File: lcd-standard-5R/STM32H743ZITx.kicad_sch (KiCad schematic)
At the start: 37 parts, among them J2 SWD, J3 Conn_ARM_JTAG_SWD_10, SW1 SW_Push, SW2 SW_Push, U10 STM32H743ZITx, Y1 25MHz, Y2 32.768KHz

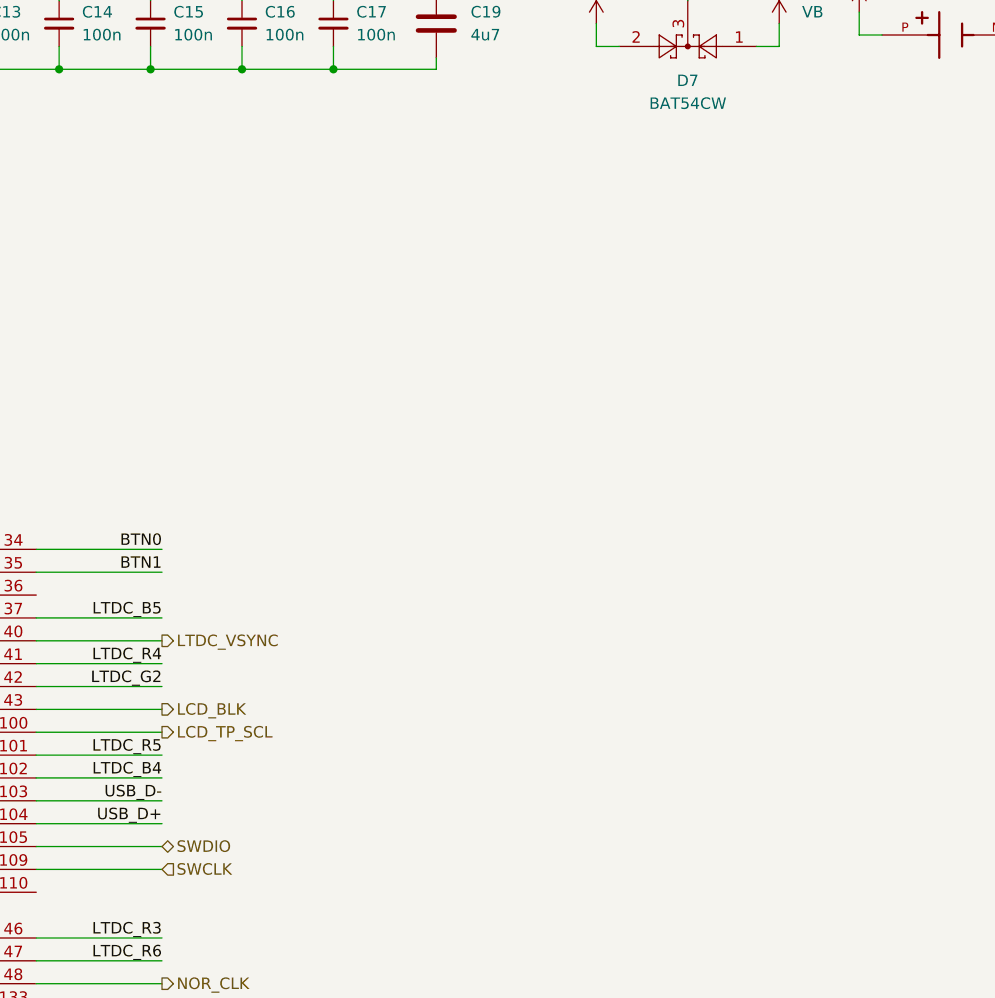
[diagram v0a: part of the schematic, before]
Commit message: Change MCU to STM32H743
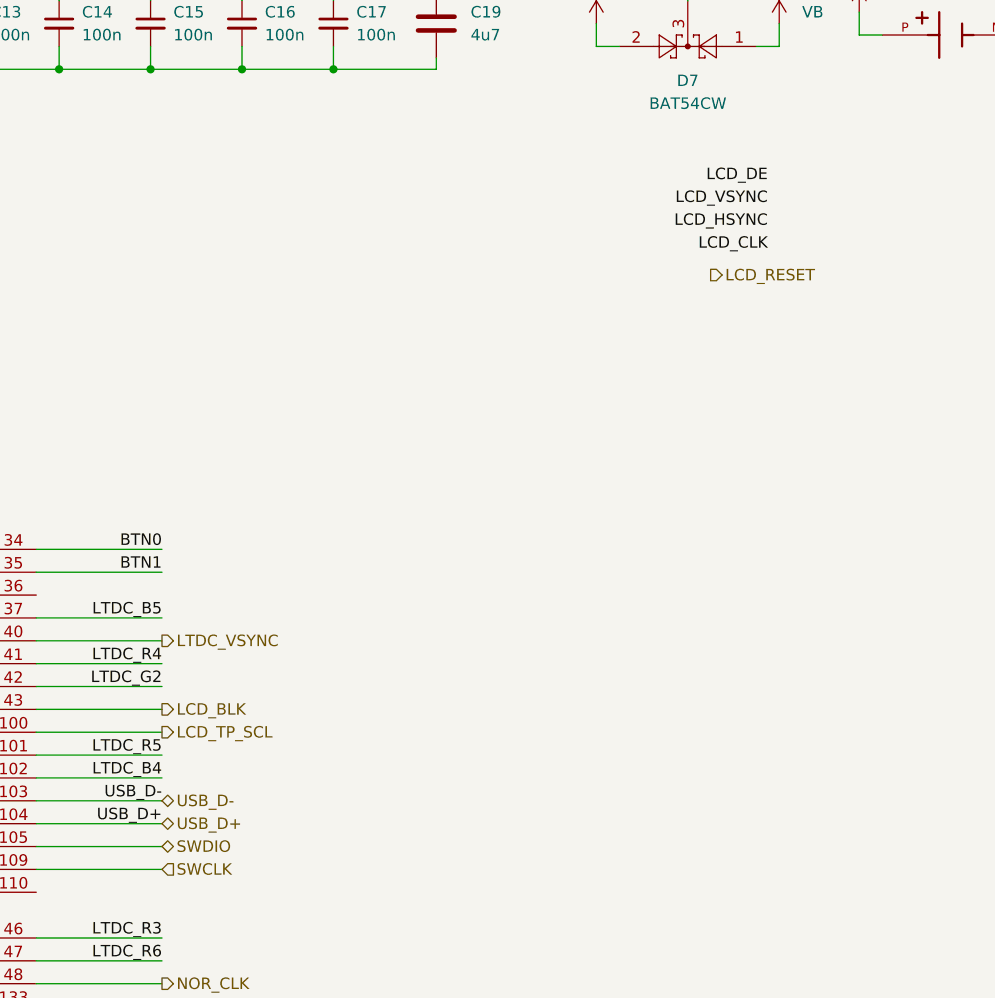
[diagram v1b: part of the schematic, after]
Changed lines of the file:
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@@
+		)
+	)
+	(label "LCD_VSYNC"
+		(at 195.58 53.34 180)
+		(fields_autoplaced yes)
+		(effects
+			(font
+				(size 1.27 1.27)
+			)
+			(justify right bottom)
 		)
 	)
@@
 		)
 	)
+	(label "LCD_DE"
+		(at 195.58 50.8 180)
+		(fields_autoplaced yes)
+		(effects
+			(font
+				(size 1.27 1.27)
+			)
+			(justify right bottom)
+		)
+	)
 	(label "LTDC_B4"
 		(at 128.27 116.84 180)
@@
 		)
 	)
+	(label "LCD_HSYNC"
+		(at 195.58 55.88 180)
+		(fields_autoplaced yes)
+		(effects
+			(font
+				(size 1.27 1.27)
+			)
+			(justify right bottom)
+		)
+	)
 	(label "OSC32_IN"
 		(at 144.78 228.6 0)
@@
 	(label "~{SDRAM_RAS}"
 		(at 283.21 60.96 180)
+		(fields_autoplaced yes)
+		(effects
+			(font
+				(size 1.27 1.27)
+			)
+			(justify right bottom)
+		)
+	)
+	(label "LCD_CLK"
+		(at 195.58 58.42 180)
 		(fields_autoplaced yes)
 		(effects
@@
 		)
 	)
+	(hierarchical_label "LCD_RESET"
+		(shape output)
+		(at 189.23 60.96 0)
+		(fields_autoplaced yes)
+		(effects
+			(font
+				(size 1.27 1.27)
+			)
+			(justify left)
+		)
+	)
 	(hierarchical_label "LTDC_G[2..7]"
 		(shape output)
@@
 		(fields_autoplaced yes)
 		(effects
+			(font
+				(size 1.27 1.27)
+			)
+			(justify left)
+		)
+	)
+	(hierarchical_label "USB_D+"
+		(shape bidirectional)
+		(at 128.27 121.92 0)
+		(fields_autoplaced yes)
+		(effects
+			(font
+				(size 1.27 1.27)
+			)
+			(justify left)
+		)
+	)
+	(hierarchical_label "USB_D-"
+		(shape bidirectional)
+		(at 128.27 119.38 0)
+		(fields_autoplaced yes)
+		(effects

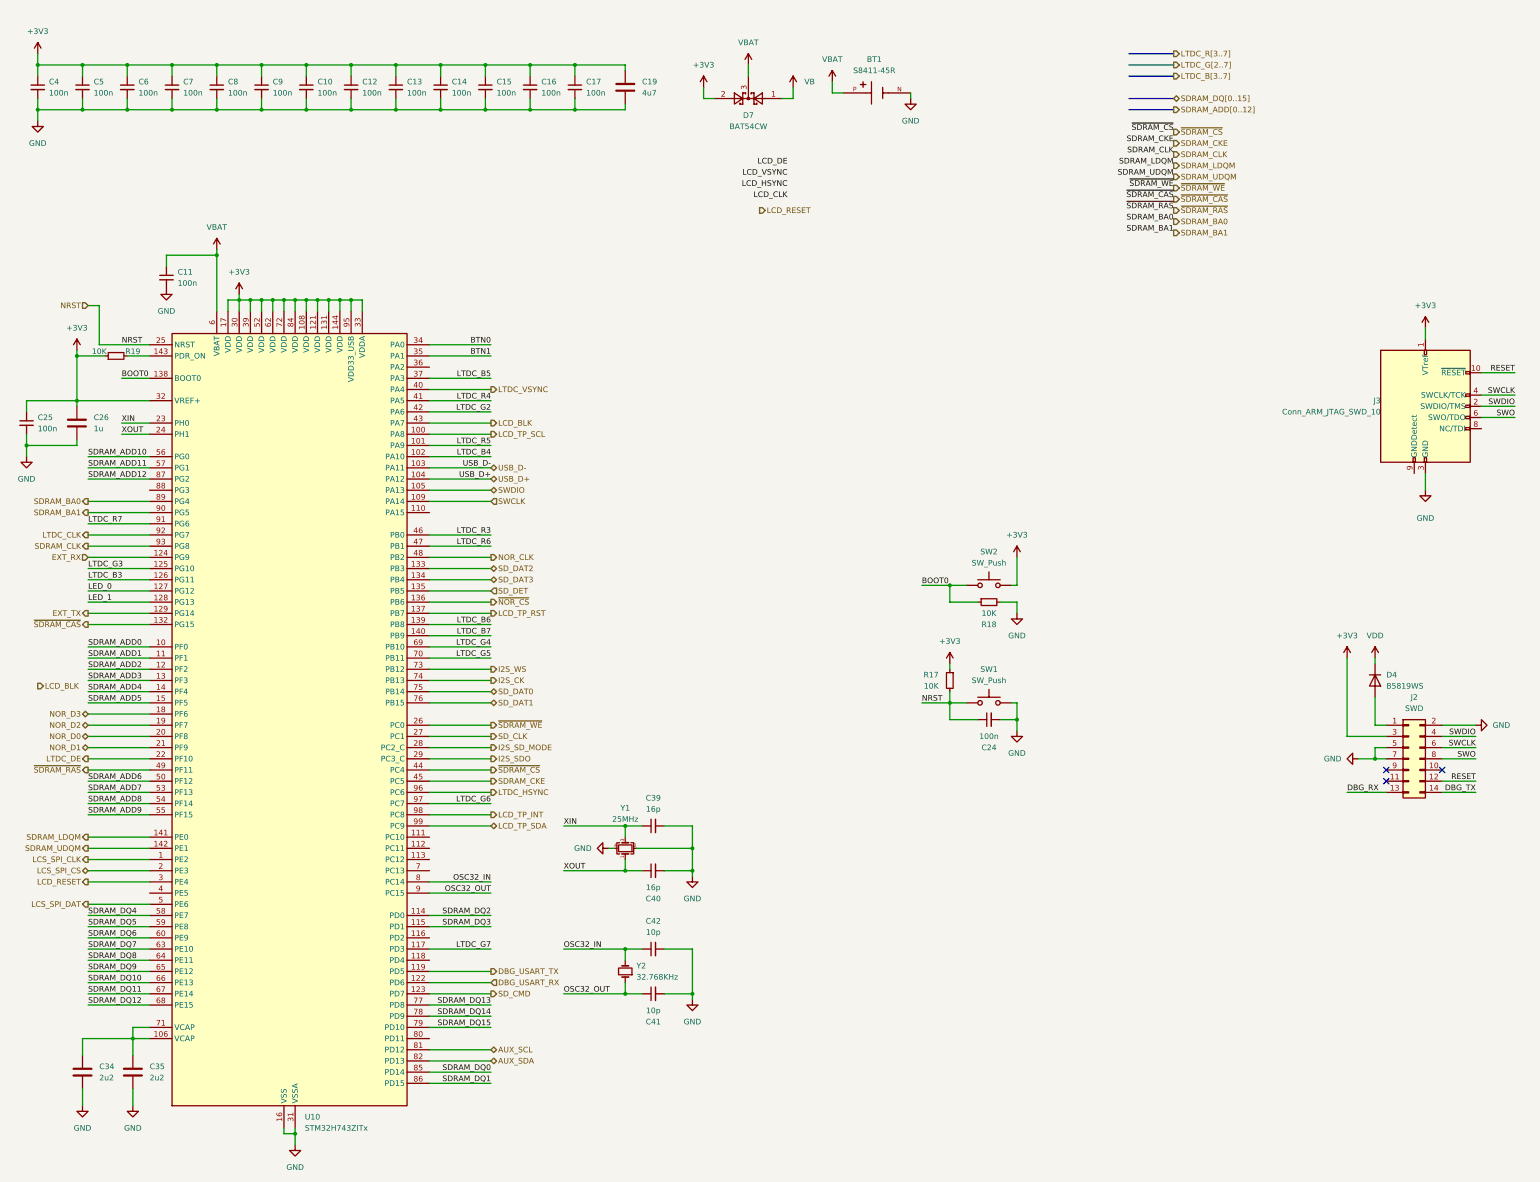
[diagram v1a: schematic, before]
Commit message: Change pinout to the optimum usage
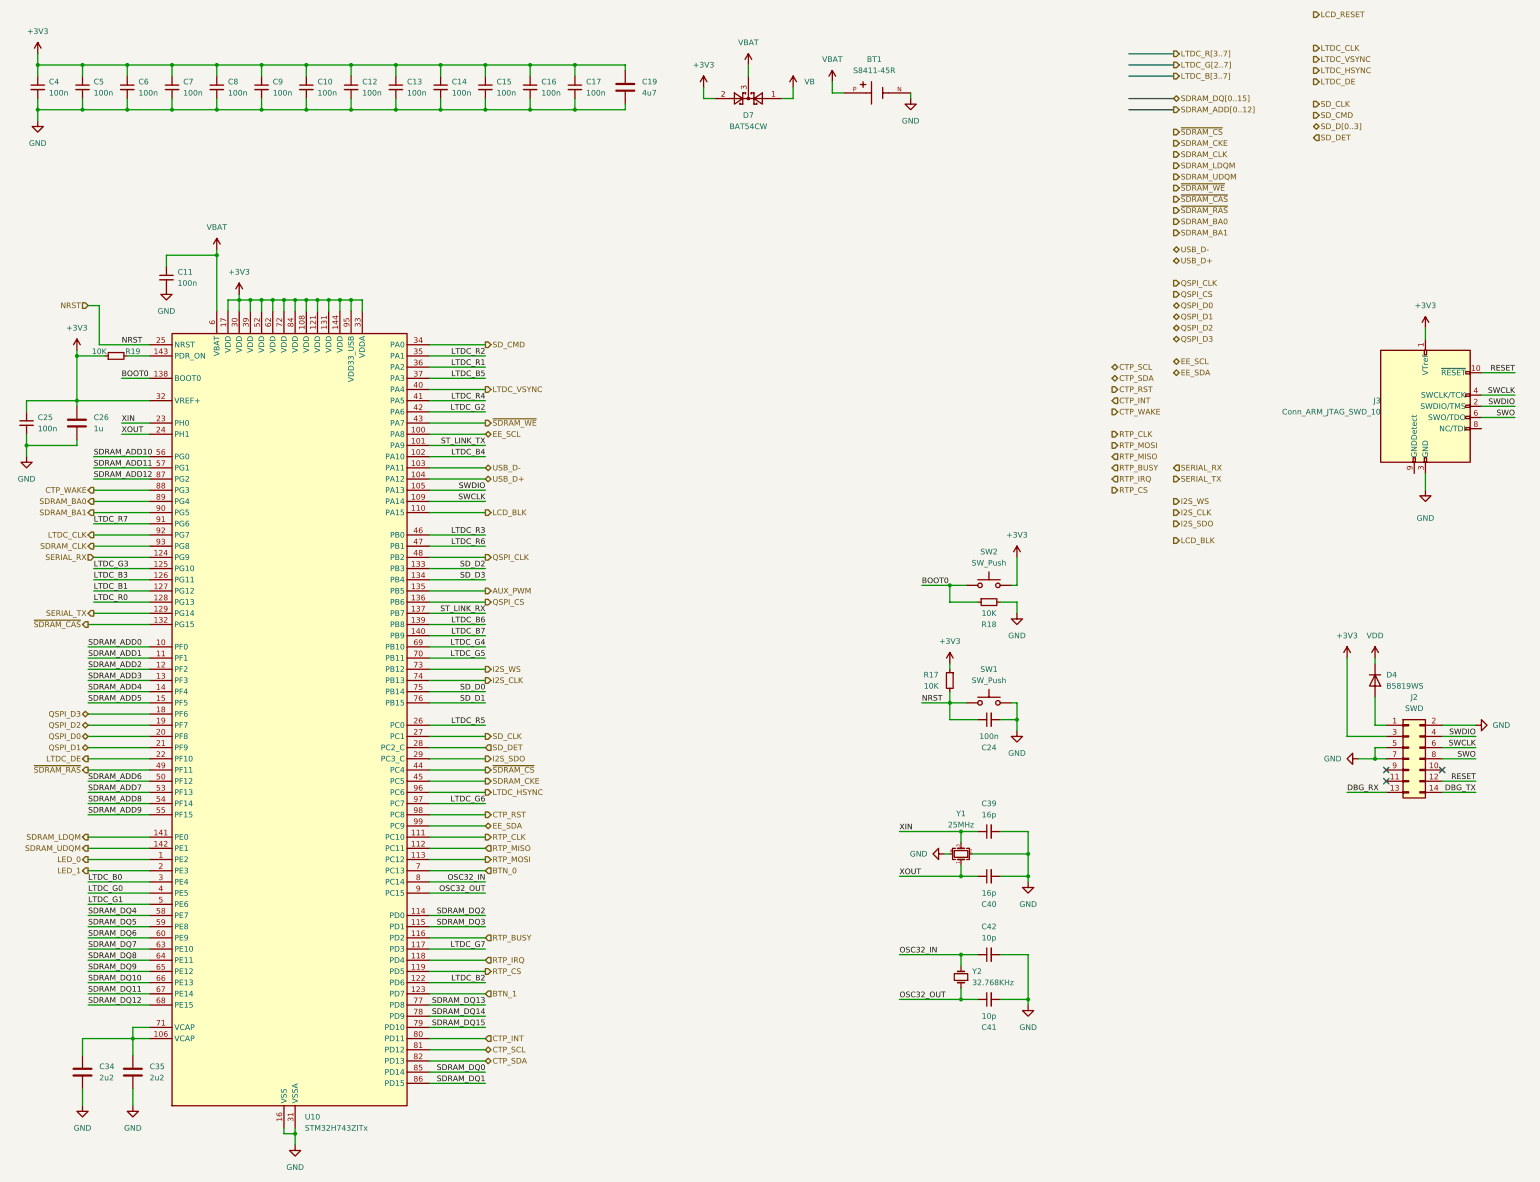
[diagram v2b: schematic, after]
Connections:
- net BTN0 is gone; now on net SD_CMD: U10.34 (PA0)
- net I2S_SD_MODE is gone; now on net SD_DET: U10.28 (PC2_C)
- net LCS_SPI_CLK is gone; now on net LED_0: U10.1 (PE2)
- net LCS_SPI_CS is gone; now on net LED_1: U10.2 (PE3)
- net LCD_BLK: now also U10.110 (PA15); no longer U10.43 (PA7)
- net LCD_RESET: no longer U10.3 (PE4)
- net LED_0: no longer U10.127 (PG12)
- net LED_1: no longer U10.128 (PG13)
- net LTDC_R5: now also U10.26 (PC0); no longer U10.101 (PA9)
- net SD_CMD: no longer U10.123 (PD7)
- net SD_DET: no longer U10.135 (PB5)
- net ~{SDRAM_WE}: now also U10.43 (PA7); no longer U10.26 (PC0)
- net RTP_CLK: now reaches U10.111 (PC10)
- net RTP_MISO: now reaches U10.112 (PC11)
- net RTP_MOSI: now reaches U10.113 (PC12)
- net RTP_BUSY: now reaches U10.116 (PD2)
- net RTP_IRQ: now reaches U10.118 (PD4)
- net LTDC_R1: now reaches U10.36 (PA2)
- net LTDC_G0: now reaches U10.4 (PE5)
- net BTN_0: now reaches U10.7 (PC13)
- net CTP_INT: now reaches U10.80 (PD11)
- net CTP_WAKE: now reaches U10.88 (PG3)
- net AUX_SCL renamed CTP_SCL
- net AUX_SDA renamed CTP_SDA
- net BTN1 renamed LTDC_R2
- net DBG_USART_RX renamed LTDC_B2
- net DBG_USART_TX renamed RTP_CS
- net EXT_RX renamed SERIAL_RX
- net EXT_TX renamed SERIAL_TX
- net I2S_CK renamed I2S_CLK
- net LCD_TP_INT renamed CTP_RST
- net LCD_TP_RST renamed ST_LINK_RX
- net LCD_TP_SCL renamed EE_SCL
- net LCD_TP_SDA renamed EE_SDA
- net LCS_SPI_DAT renamed LTDC_G1
- net NOR_CLK renamed QSPI_CLK
- net NOR_D0 renamed QSPI_D0
- net NOR_D1 renamed QSPI_D1
- net NOR_D2 renamed QSPI_D2
- net NOR_D3 renamed QSPI_D3
- net SD_DAT0 renamed SD_D0
- net SD_DAT1 renamed SD_D1
- net SD_DAT2 renamed SD_D2
- net SD_DAT3 renamed SD_D3
- net ~{NOR_CS} renamed QSPI_CS
- new net AUX_PWM: U10.135 (PB5)
- new net BTN_1: U10.123 (PD7)
- new net LTDC_B0: U10.3 (PE4)
- new net LTDC_B1: U10.127 (PG12)
- new net LTDC_R0: U10.128 (PG13)
- new net ST_LINK_TX: U10.101 (PA9)
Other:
- moved on the sheet: C39, C40, C41, C42, Y1, Y2

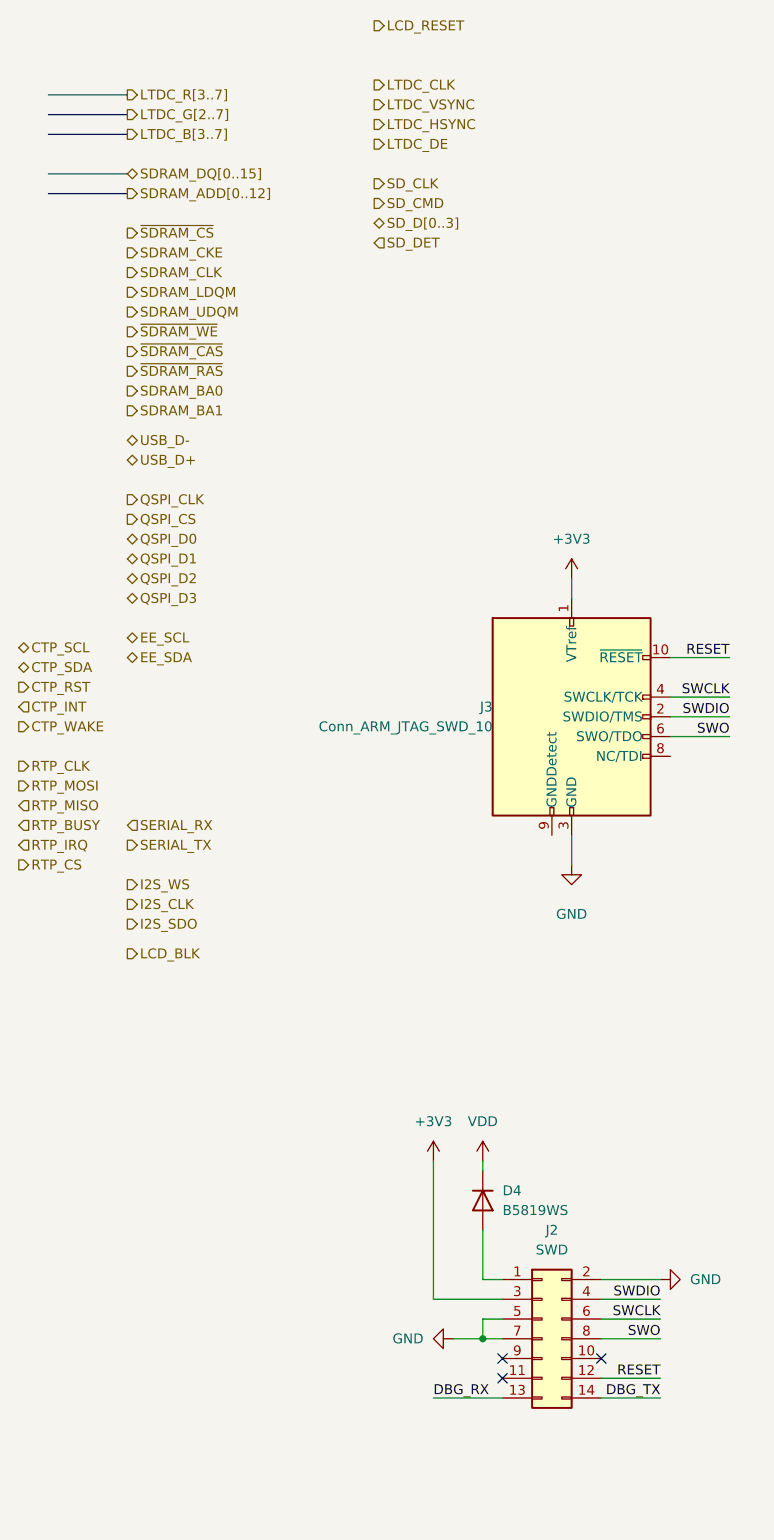
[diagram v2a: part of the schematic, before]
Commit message: Finished SDRAM, LCD (need checkup with CubeIDE), RTP touch controll
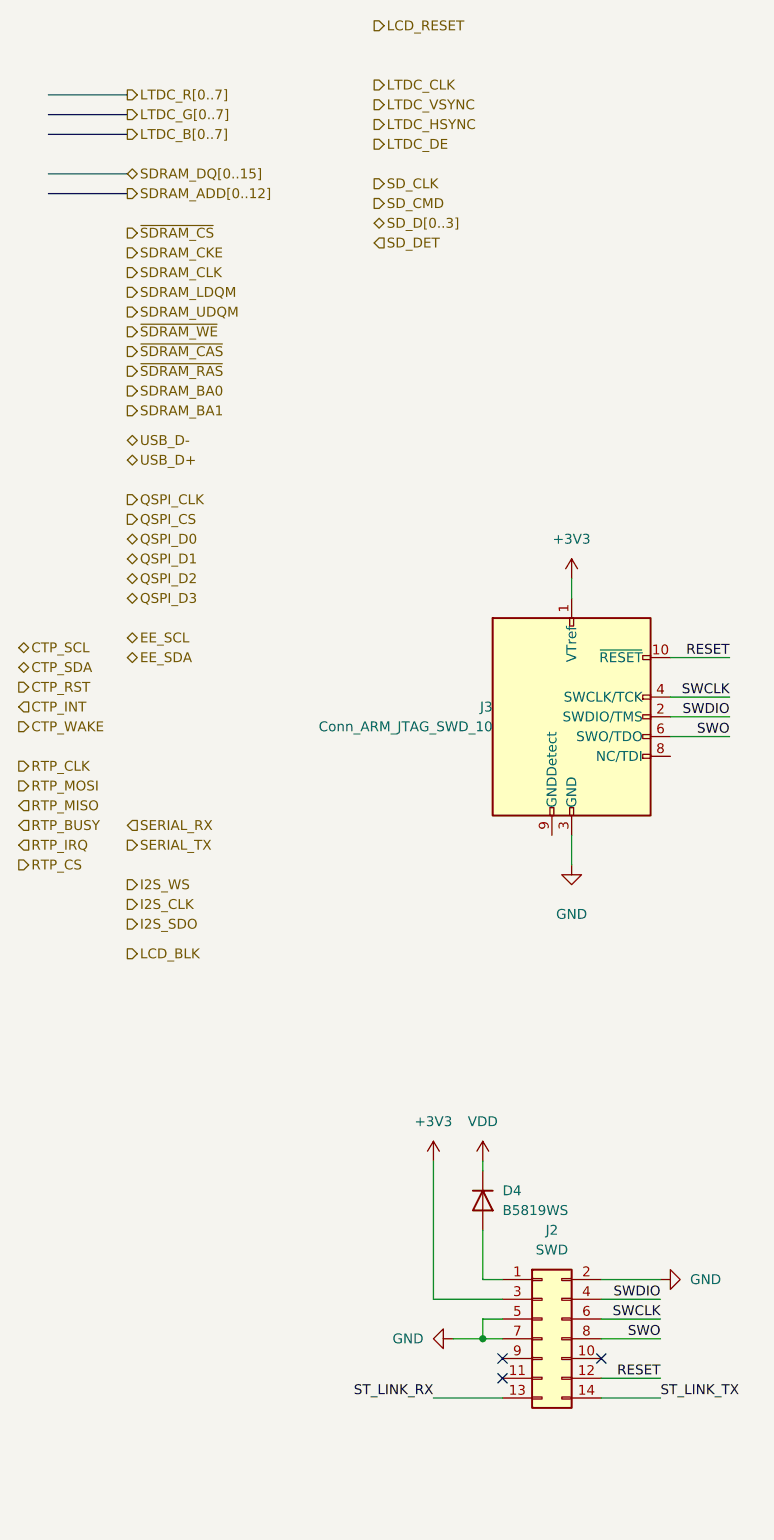
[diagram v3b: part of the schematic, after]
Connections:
- net DBG_RX is gone; now on net ST_LINK_RX: J2.13 (Pin_13)
- net DBG_TX is gone; now on net ST_LINK_TX: J2.14 (Pin_14)
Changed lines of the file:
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@@
+		)
+	)
+	(label "ST_LINK_TX"
+		(at 351.79 193.04 0)
+		(fields_autoplaced yes)
+		(effects
+			(font
+				(size 1.27 1.27)
+			)
+			(justify left bottom)
 		)
 	)
@@
 		)
 	)
-	(label "DBG_RX"
-		(at 322.58 193.04 0)
-		(fields_autoplaced yes)
-		(effects
-			(font
-				(size 1.27 1.27)
-			)
-			(justify left bottom)
-		)
-	)
 	(label "SDRAM_ADD3"
 		(at 36.83 167.64 0)
@@
 		)
 	)
+	(label "ST_LINK_RX"
+		(at 322.58 193.04 180)
+		(fields_autoplaced yes)
+		(effects
+			(font
+				(size 1.27 1.27)
+			)
+			(justify right bottom)
+		)
+	)
 	(label "ST_LINK_TX"
 		(at 127 114.3 180)
@@
 	(label "SWDIO"
 		(at 127 124.46 180)
-		(fields_autoplaced yes)
-		(effects
-			(font
-				(size 1.27 1.27)
-			)
-			(justify right bottom)
-		)
-	)
-	(label "DBG_TX"
-		(at 351.79 193.04 180)
 		(fields_autoplaced yes)
 		(effects
@@
 		)
 	)
+	(hierarchical_label "LTDC_G[0..7]"
+		(shape output)
+		(at 283.21 27.94 0)
+		(fields_autoplaced yes)
+		(effects
+			(font
+				(size 1.27 1.27)
+			)
+			(justify left)
+		)
+	)
 	(hierarchical_label "LTDC_HSYNC"
 		(shape output)
@@
 		)
 	)
+	(hierarchical_label "LTDC_R[0..7]"
+		(shape output)
+		(at 283.21 25.4 0)
+		(fields_autoplaced yes)
+		(effects
+			(font
+				(size 1.27 1.27)
+			)
+			(justify left)
+		)
+	)
 	(hierarchical_label "SDRAM_CLK"
 		(shape output)
@@
 		(shape output)
 		(at 314.96 16.51 0)
-		(fields_autoplaced yes)
-		(effects
-			(font
-				(size 1.27 1.27)
-			)
-			(justify left)
-		)
-	)
-	(hierarchical_label "LTDC_G[2..7]"
-		(shape output)
-		(at 283.21 27.94 0)
-		(fields_autoplaced yes)
-		(effects
-			(font
-				(size 1.27 1.27)
-			)
-			(justify left)
-		)
-	)
-	(hierarchical_label "LTDC_B[3..7]"
-		(shape output)
-		(at 283.21 30.48 0)
 		(fields_autoplaced yes)
 		(effects
@@
 		)
 	)
-	(hierarchical_label "LTDC_R[3..7]"
-		(shape output)
-		(at 283.21 25.4 0)
-		(fields_autoplaced yes)
-		(effects
+	(hierarchical_label "LTDC_B[0..7]"
+		(shape output)
+		(at 283.21 30.48 0)
+		(fields_autoplaced yes)
+		(effects

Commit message: Finsihed, need to touch up a bit
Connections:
- net RESET is gone; now on net NRST: J2.12 (Pin_12), J3.10 (~{RESET})
- net CTP_SCL: now also U10.100 (PA8); no longer U10.81 (PD12)
- net CTP_SDA: now also U10.99 (PC9); no longer U10.82 (PD13)
- net EE_SCL: now also U10.81 (PD12); no longer U10.100 (PA8)
- net EE_SDA: now also U10.82 (PD13); no longer U10.99 (PC9)
- net VB: now also BT1.P
- net VBAT: no longer BT1.P
- net SWO: no longer names the net of J2.8 (Pin_8)
- net SWO: no longer J3.6 (SWO/TDO)
- no-connect marks 3 -> 6
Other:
- moved on the sheet: BT1
